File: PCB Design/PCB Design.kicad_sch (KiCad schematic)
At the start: 48 parts, among them J2 DX07S024WJ3R400, J4 Conn_02x16_Odd_Even, Q1 2N7002, Q2 2N7002, Q3 PN2222A, U1 INA219AxD, U10 LD1117S50TR_SOT223, U2 IP2721, U3 DRV8833PW, U4 AP22818AKEWT, U5 AP22818AKEWT, U6 DRV8833PW, U7 BQ21040DBV, U8 LD1117S33TR_SOT223

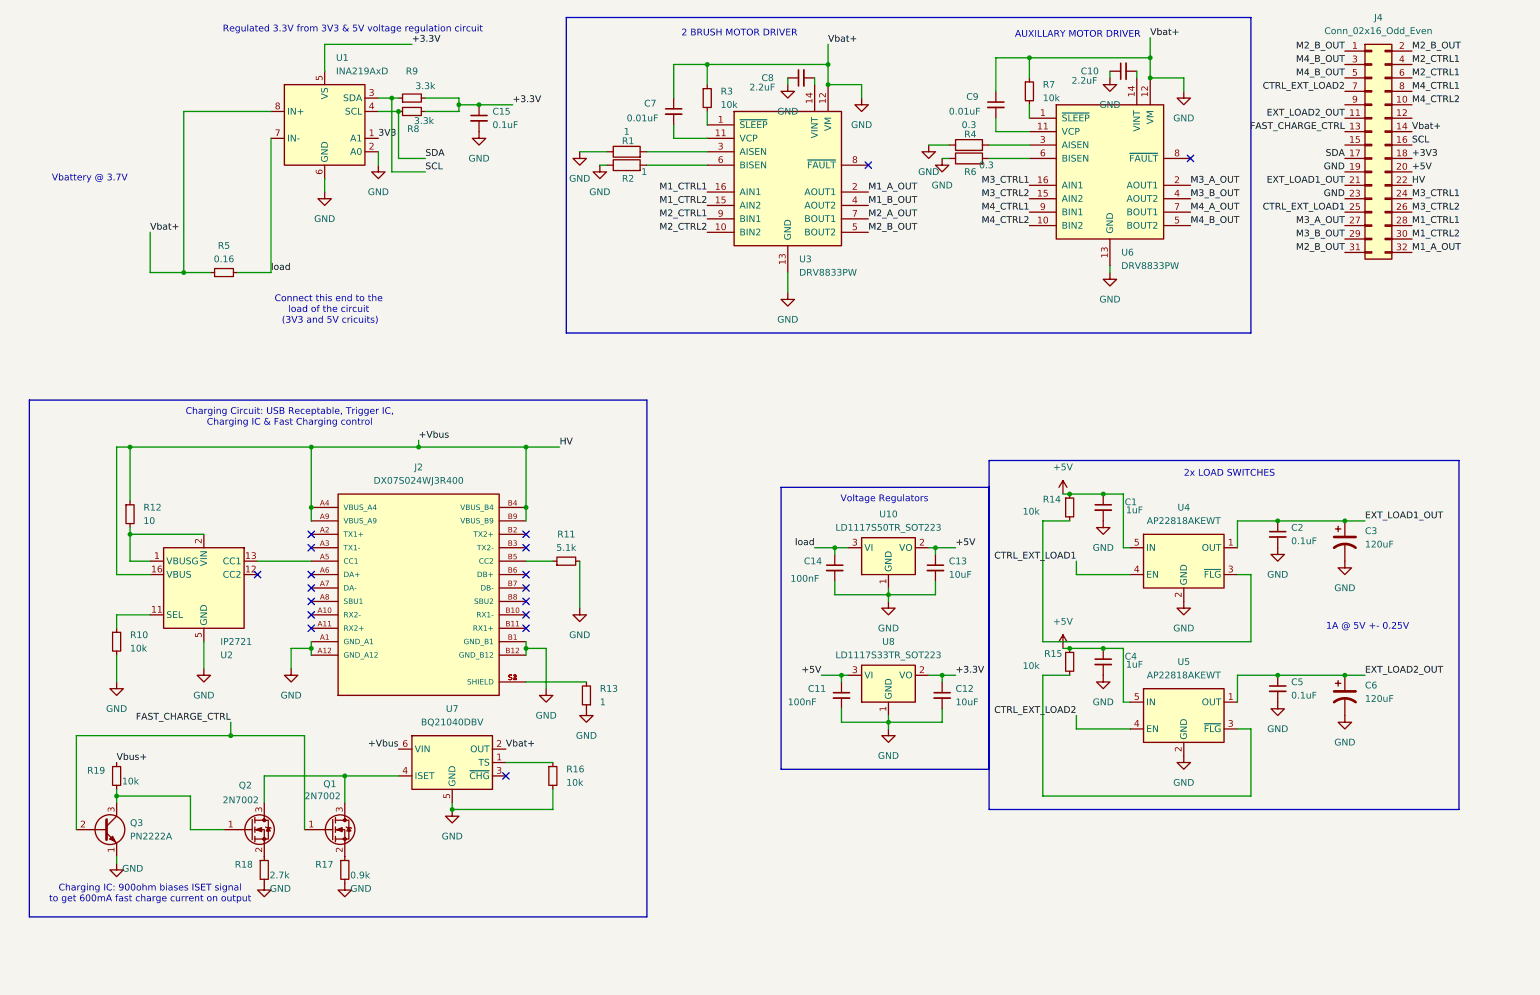
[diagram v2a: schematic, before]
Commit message: Update voltage regulator and boost converter circuits.
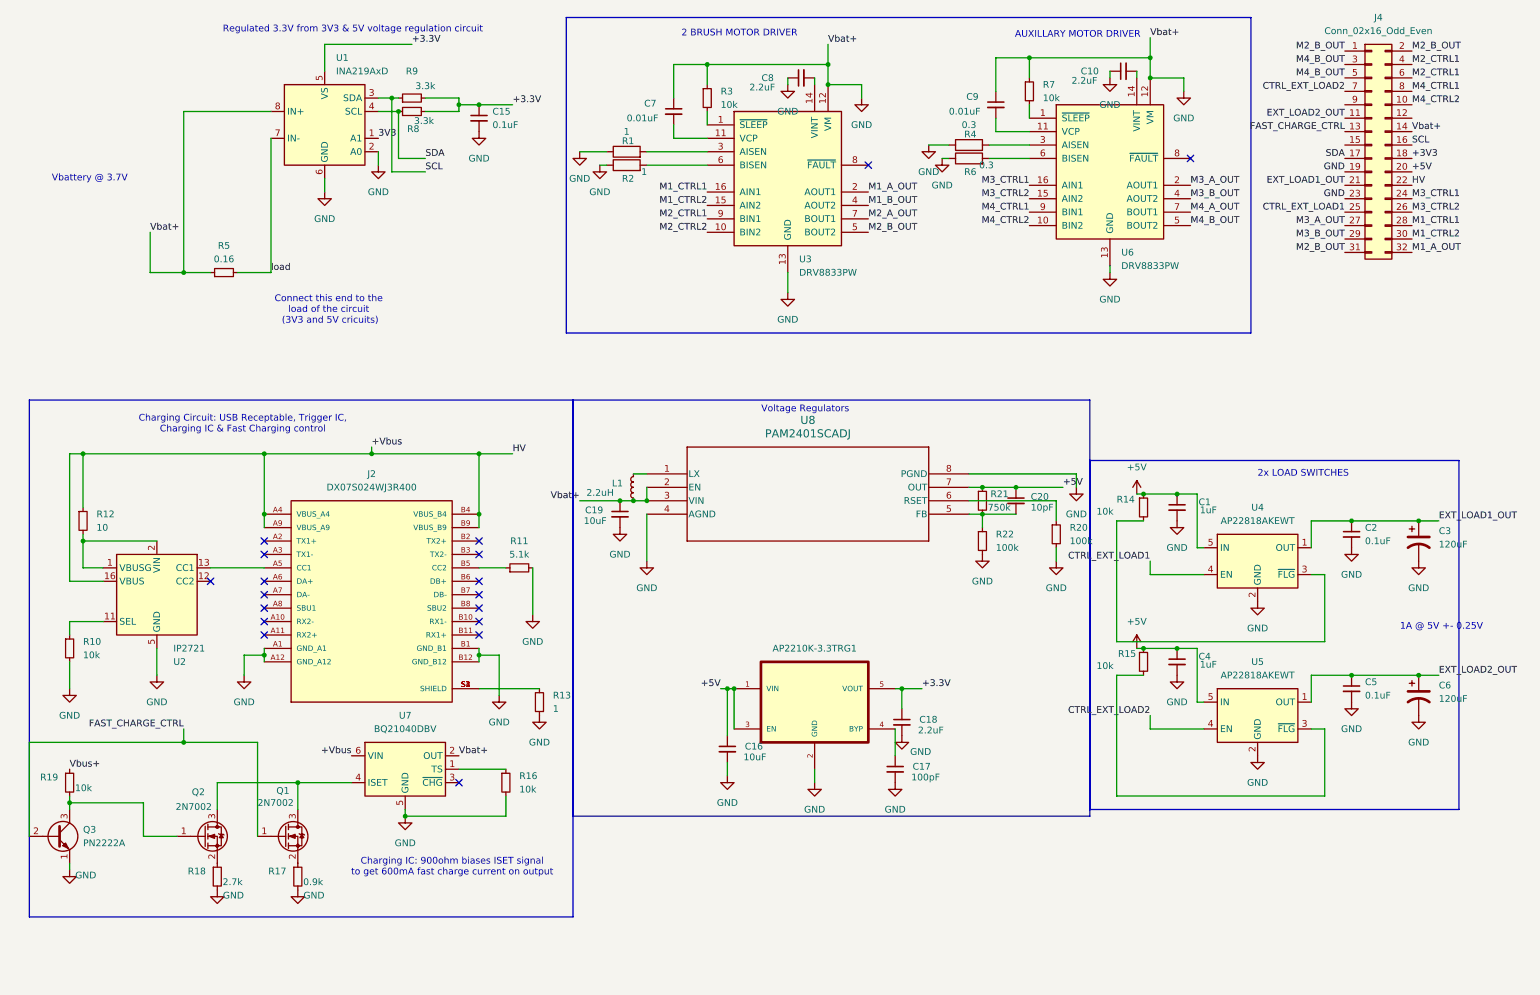
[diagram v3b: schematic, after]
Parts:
- removed C11, C14: 100nF, symbol Device:C_Small
- removed C12, C13: 10uF, symbol Device:C_Small
- removed U10: LD1117S50TR_SOT223, Package_TO_SOT_SMD:SOT-223-3_TabPin2, symbol Regulator_Linear:LD1117S50TR_SOT223
- removed U8: LD1117S33TR_SOT223, Package_TO_SOT_SMD:SOT-223-3_TabPin2, symbol Regulator_Linear:LD1117S33TR_SOT223
- added C16, C19: 10uF, symbol Device:C_Small
- added C17: 100pF, symbol Device:C_Small
- added C18: 2.2uF, symbol Device:C_Small
- added C20: 10pF, symbol Device:C_Small
- added L1: 2.2uH, symbol Device:L_Small
- added R20, R22: 100k, symbol Device:R_Small
- added R21: 750k, symbol Device:R_Small
- added U11: AP2210K-3.3TRG1, AP2210K-3.3TRG1:SOT-23-5_RAW, symbol AP2210K-3.3TRG1:AP2210K-3.3TRG1
- added U8: PAM2401SCADJ, MSOP8_DIO, symbol PAM:PAM2401SCADJ
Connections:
- net +3.3V: now also C18.1, U11.5 (VOUT)
- net +5V: now also C16.1, C20.1, R21.1, U11.1 (VIN), U11.3 (EN), U8.7 (OUT)
- net GND: now also C16.2, C17.2, C18.2, C19.1, C19.2, L1.1, R20.2, R22.2, U11.2 (GND), U8.2 (EN), U8.3 (VIN), U8.4 (AGND), U8.8 (PGND)
- new net: C20.2, R21.2, R22.1, U8.5 (FB)
- new net: C17.1, U11.4 (BYP)
- new net: L1.2, U8.1 (LX)
- new net: R20.1, U8.6 (RSET)
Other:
- moved on the sheet: C1, C2, C3, C4, C5, C6, J2, Q1, Q2, Q3, R10, R11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
